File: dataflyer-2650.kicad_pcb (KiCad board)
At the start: 2 copper layers, 79 x 26 mm, 2 parts, among them J1 26-pin IDC (Dataflyer side), J2 50-pin IDC (SCSI chain out)

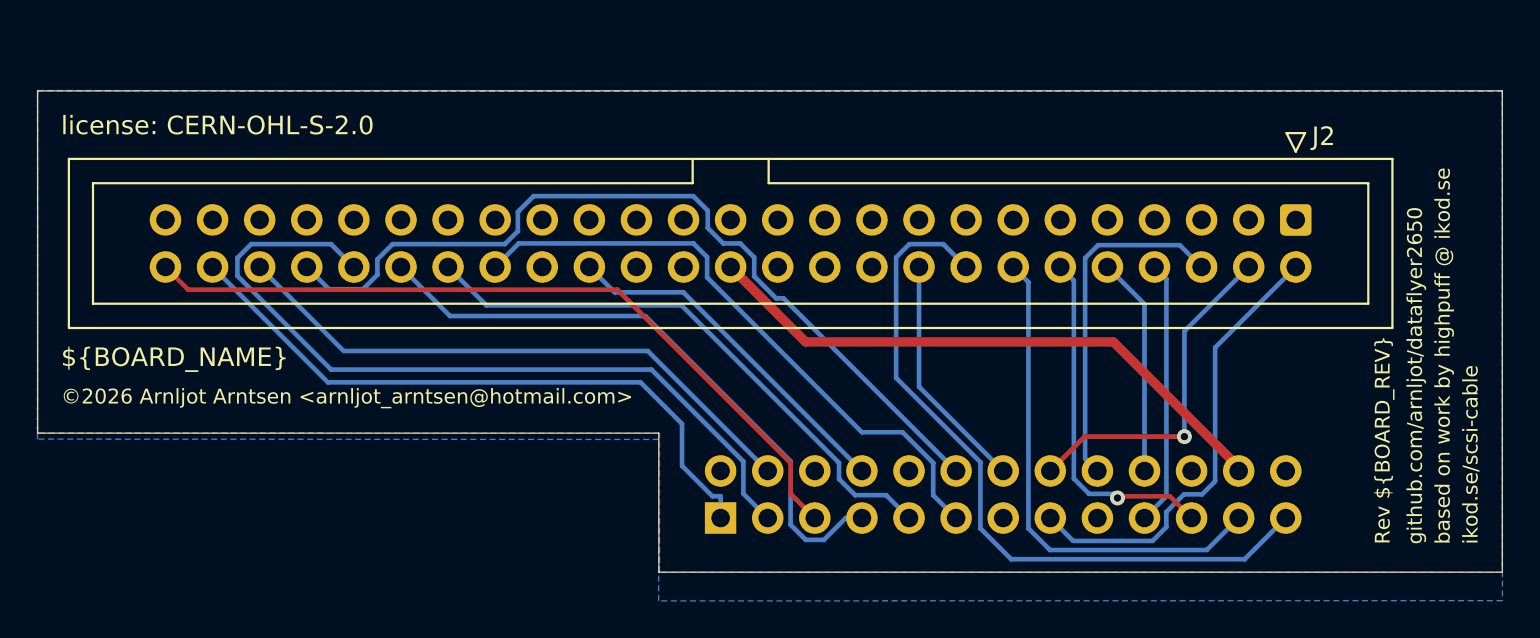
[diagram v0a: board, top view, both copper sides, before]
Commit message: 1.3: match front/back board outline (overlapping step edges)
In 1.2 the front and back board-edge outlines did not match: the two
horizontal step edges that run parallel to the connectors did not
overlap between the F and B sides. The lower-right tab edge has been
corrected so both sides now share the same outline.

No schematic or pinout change - electrically identical to 1.2, same
reverse-L design. Gerbers + drill re-exported from KiCad 10.0.3; the
metadata now correctly reports revision 1.3 (the 1.2.1 title-block fix
is now reflected in the exported files).

BOARD_REV bumped to 1.3. Bundled zip (dataflyer-2650-v1.3.zip) prepared
for PCBWay. README revision history updated; Files section rev numbers
synced.

(c) 2026 Arnljot Arntsen
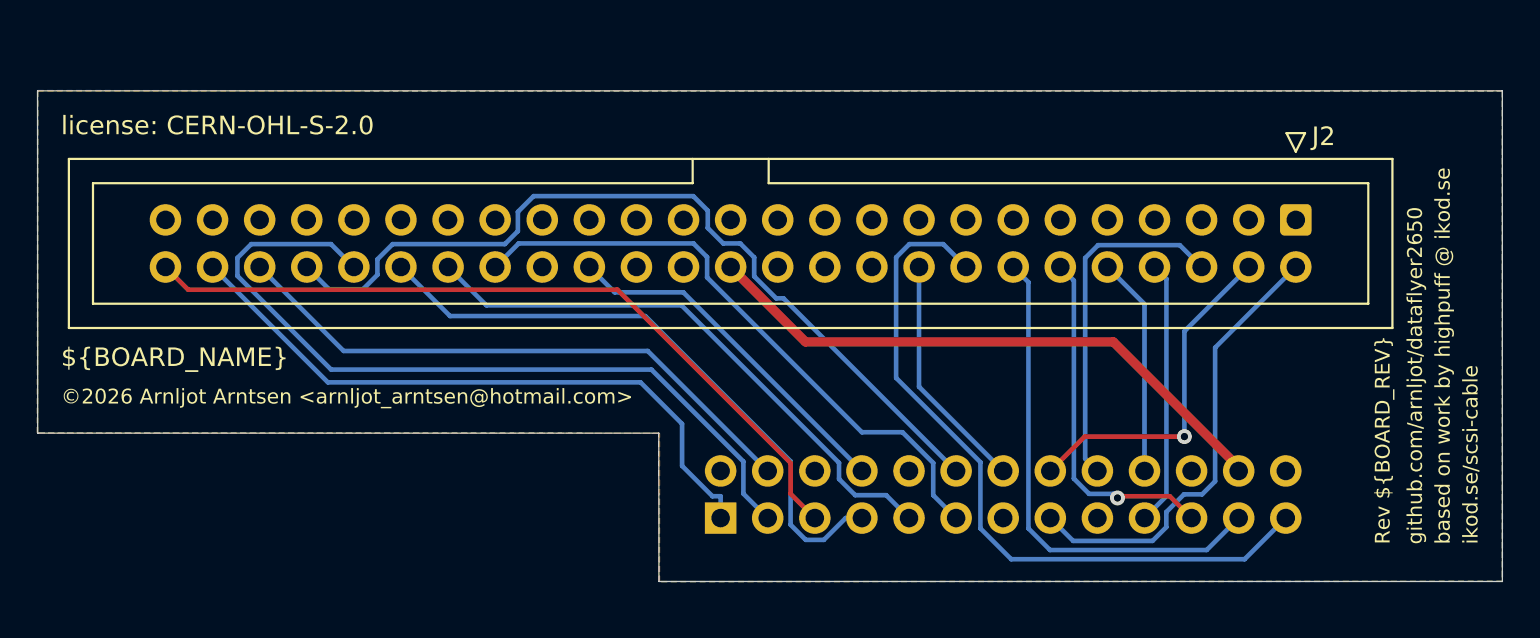
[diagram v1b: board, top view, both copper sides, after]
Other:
- board size 79 x 26 mm -> 79 x 26.5 mm
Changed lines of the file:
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@@
 	)
 	(property "BOARD_NAME" "DataFlyer 2650 — 26-pin to 50-pin SCSI Adapter")
-	(property "BOARD_REV" "1.2.1")
+	(property "BOARD_REV" "1.3")
 	(footprint "Connector_IDC:IDC-Header_2x25_P2.54mm_Vertical"
 		(layer "F.Cu")
@@
 	(gr_line
 		(start 128.744019 111.5)
-		(end 128.74992 119)
+		(end 128.75496 119.5)
 		(stroke
 			(width 0.05)
@@
 	(gr_line
 		(start 174.24 93.04)
-		(end 174.24 119)
+		(end 174.24 119.5)
 		(stroke
 			(width 0.05)
@@
 	)
 	(gr_line
-		(start 174.24 119)
-		(end 128.74992 119)
+		(start 174.24504 119.5)
+		(end 128.75496 119.5)
 		(stroke
 			(width 0.05)
@@
 		(polygon
 			(pts
-				(xy 174.240002 118.994424) (xy 128.784353 119.00557) (xy 128.782516 111.51147) (xy 95.23354 111.48854)
+				(xy 174.240002 119.494424) (xy 128.784476 119.50557) (xy 128.782516 111.51147) (xy 95.23354 111.48854)
 				(xy 95.246165 93.039972) (xy 174.239986 93.039976)
 			)
@@
 		(polygon
 			(pts
-				(xy 174.244417 120.533941) (xy 128.73984 120.54884) (xy 128.744019 111.841537) (xy 95.234578 111.821966)
+				(xy 174.244076 119.492554) (xy 128.74034 119.507454) (xy 128.744178 111.50978) (xy 95.234772 111.490208)
 				(xy 95.245559 93.023994) (xy 174.235421 93.05521)
 			)

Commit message: 1.4: manual route to fix unconnected J1 pin 22; document DataFlyer mirror
PCBWay flagged that J1 pin 22 was not connected on the 1.3 board. The
board has been manually routed to close the gap. Board now measures
~79 x 27 mm (reverse-L outline with a small lower-left cut-out).

Newly documented incompatibility: the Expansion Systems DataFlyer 1200
SCSI+ presents its 26-pin header mirrored relative to the Phase5
Blizzard - the pinout is identical, but the odd-pin and even-pin rows
are swapped. The board is routed for the Blizzard orientation and will
NOT work with the DataFlyer without rework. A compatibility note has
been added to the top of the README.

Test status corrected: only v1.1 has been bench-tested on real hardware
(with the Blizzard SCSI kit). v1.2-v1.4 are outline/routing fixes that
have not been re-tested; the earlier "1.2 tested working" wording has
been removed from the revision history.

Pinout unchanged - routing fix only. BOARD_REV bumped to 1.4; Gerbers +
drill re-exported (metadata correctly reports rev 1.4). Bundled zip
(dataflyer-2650-v1.4.zip) prepared for PCBWay. README updated; Files
section rev numbers synced.

(c) 2026 Arnljot Arntsen
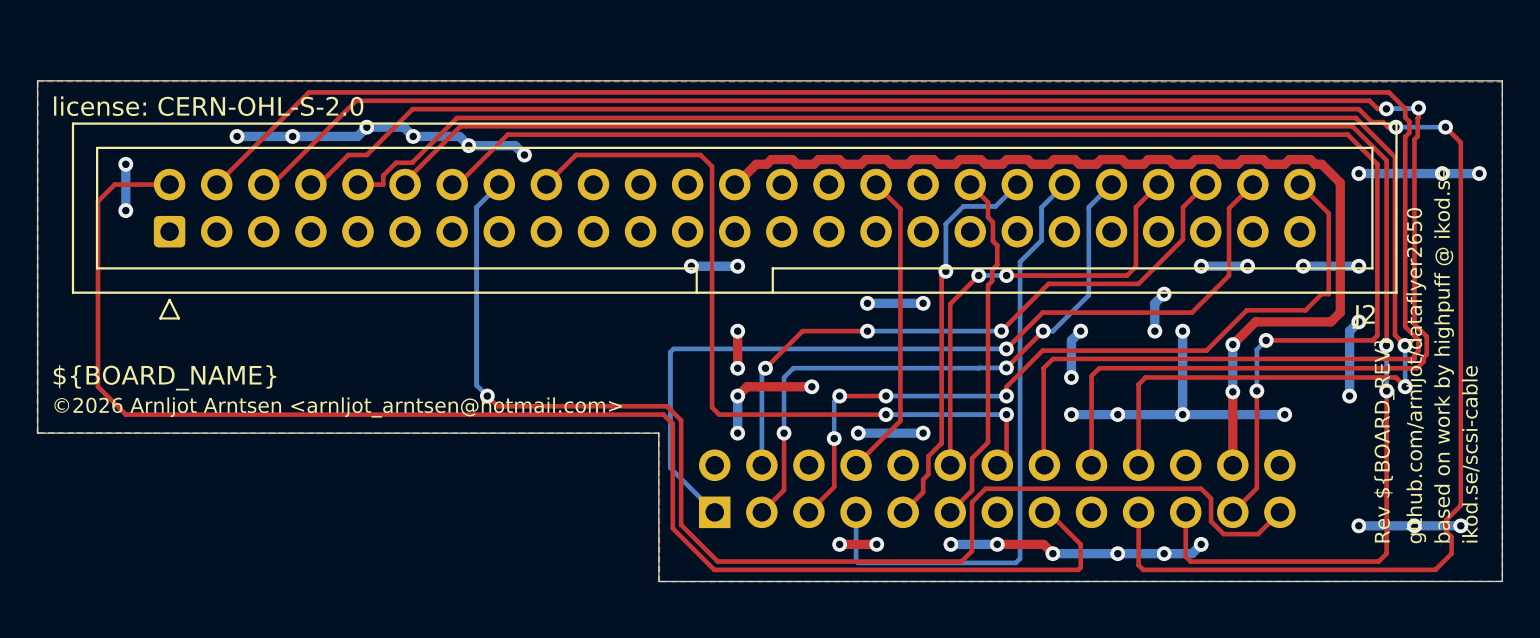
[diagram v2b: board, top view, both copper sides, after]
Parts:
- moved J2 60.7 mm to (102.4, 100.6), turned to 90 degrees
- moved J1 0.44 mm to (131.8, 115.8)
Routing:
- net GND: track 0.00 -> 94.6 mm, vias 0 -> 48
- net DB3: track 14.3 -> 107.3 mm, vias 0 -> 2
- net DB1: track 18.6 -> 106.0 mm, vias 1 -> 0
- net DB2: track 18.8 -> 101.6 mm, vias 0 -> 2
- net DB4: track 11.8 -> 90.3 mm, vias 0 -> 2
- net DB5: track 19.0 -> 89.8 mm, vias 1 -> 2
- net DB0: track 24.6 -> 78.6 mm
- net DB6: track 27.0 -> 77.1 mm, vias 0 -> 2
- net DBP: track 12.9 -> 41.8 mm, vias 0 -> 2
- net DB7: track 39.2 -> 67.3 mm, vias 0 -> 1
- net TERMPWR: track 32.1 -> 56.1 mm, vias 0 -> 2
- net SEL: track 46.0 -> 24.5 mm, vias 0 -> 2
- net BSY: track 33.2 -> 19.3 mm
- net REQ: track 35.0 -> 46.9 mm, vias 0 -> 1
- net MSG: track 43.1 -> 32.5 mm, vias 0 -> 3
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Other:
- board size 79 x 26.5 mm -> 79 x 27 mm
